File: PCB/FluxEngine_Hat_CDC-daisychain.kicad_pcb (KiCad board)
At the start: 2 copper layers, 83.3 x 24.1 mm, 3 parts, among them J1 CY8CKIT-059, P1 FDC_BUS_IBMPC, P2 FDC_BUS_CDC_DaisyChain

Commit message: silkscreen, pics
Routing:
- net GND: vias 15 -> 17

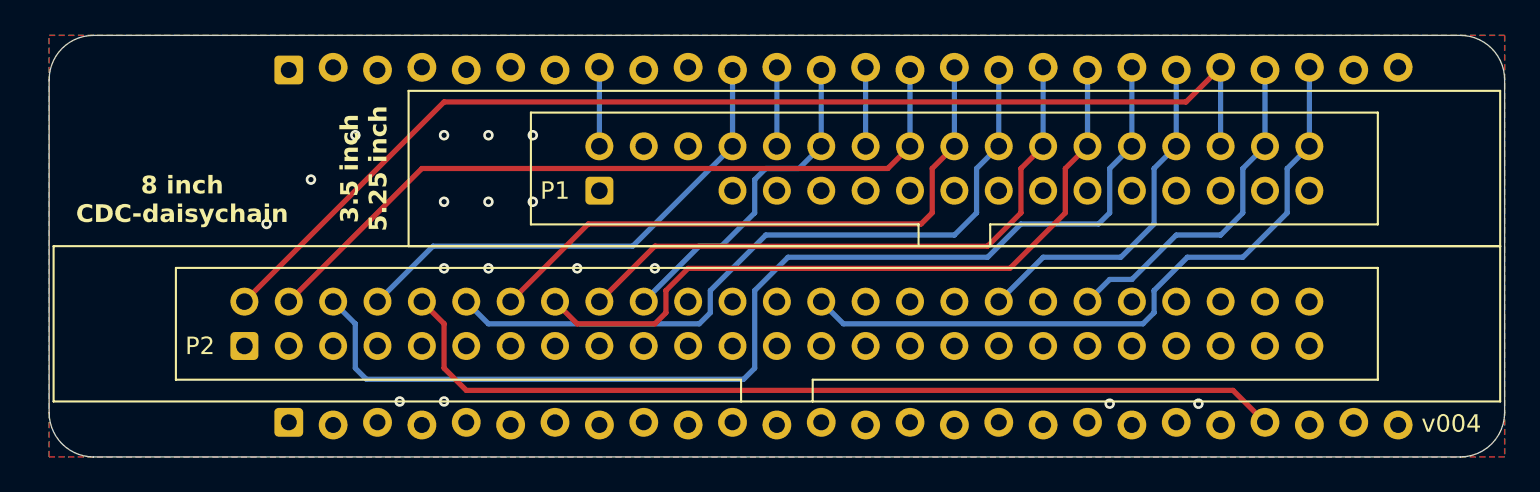
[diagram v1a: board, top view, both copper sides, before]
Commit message: reduce thermal spoke width
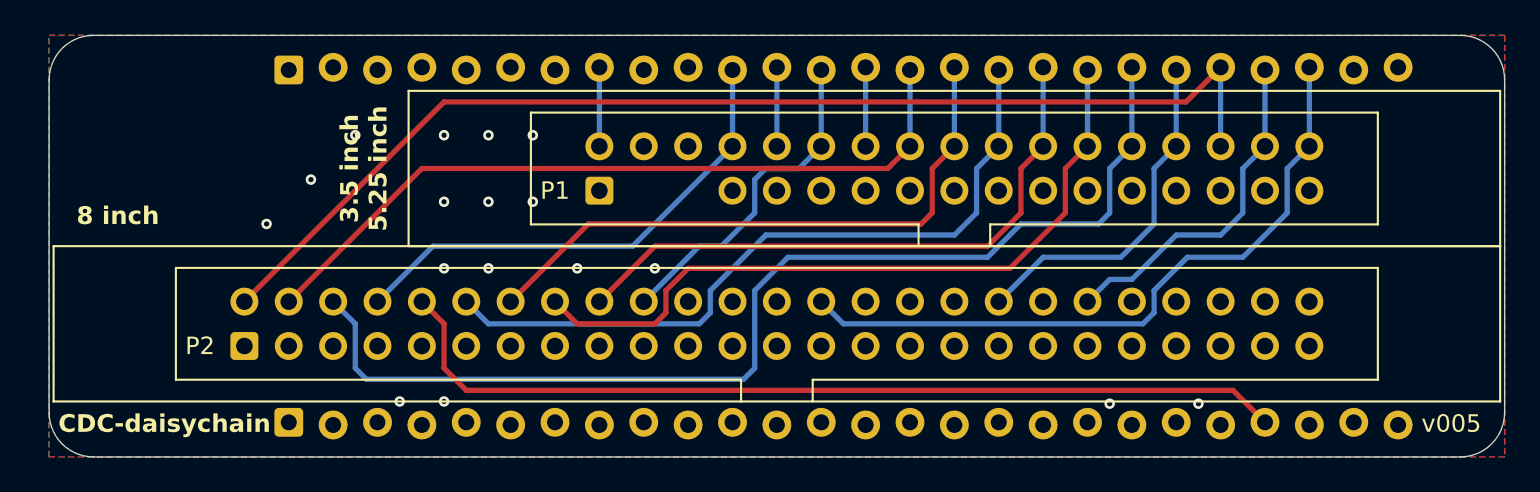
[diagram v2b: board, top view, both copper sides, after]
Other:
- board text added: "8 inch"
- board text added: "CDC-daisychain"
- board text removed: "8 inch CDC-daisychain"

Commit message: staggered rows offset & direction
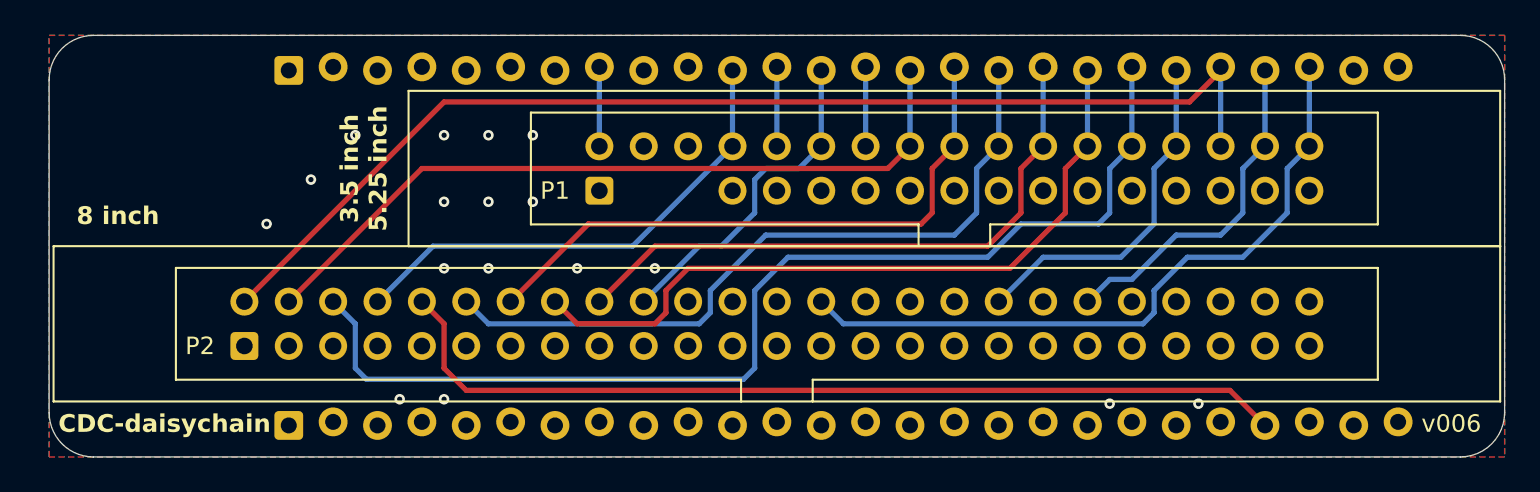
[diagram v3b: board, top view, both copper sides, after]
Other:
- board text added: "CY8CKIT-059 this side face up"
- board text removed: "CY8CKIT-059 usb & button face away from hat"
